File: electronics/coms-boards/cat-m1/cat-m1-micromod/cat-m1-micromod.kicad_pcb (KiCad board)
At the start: 2 copper layers, 37.5 x 65 mm, 56 parts, among them J1 MICROMOD_FUNCTION__STANDARD, J2 CONUFL001-SMD-T, J3 USB4145-03-0230-C_REVA, J4 SIM8060-6-0-14-00-A, Q1 BC847, Q2 BC847, SW1 1977223-6, U1 TPS22967DSGR, U2 SARA-R410M-02B, U3 AOZ8904CIL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

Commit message: updated to re-align with master
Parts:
- R2: value 1K -> 500
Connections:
- J1 pad 59: unconnected-(J1-Pad59) -> GND
- J1 pad 61: unconnected-(J1-Pad61) -> GND

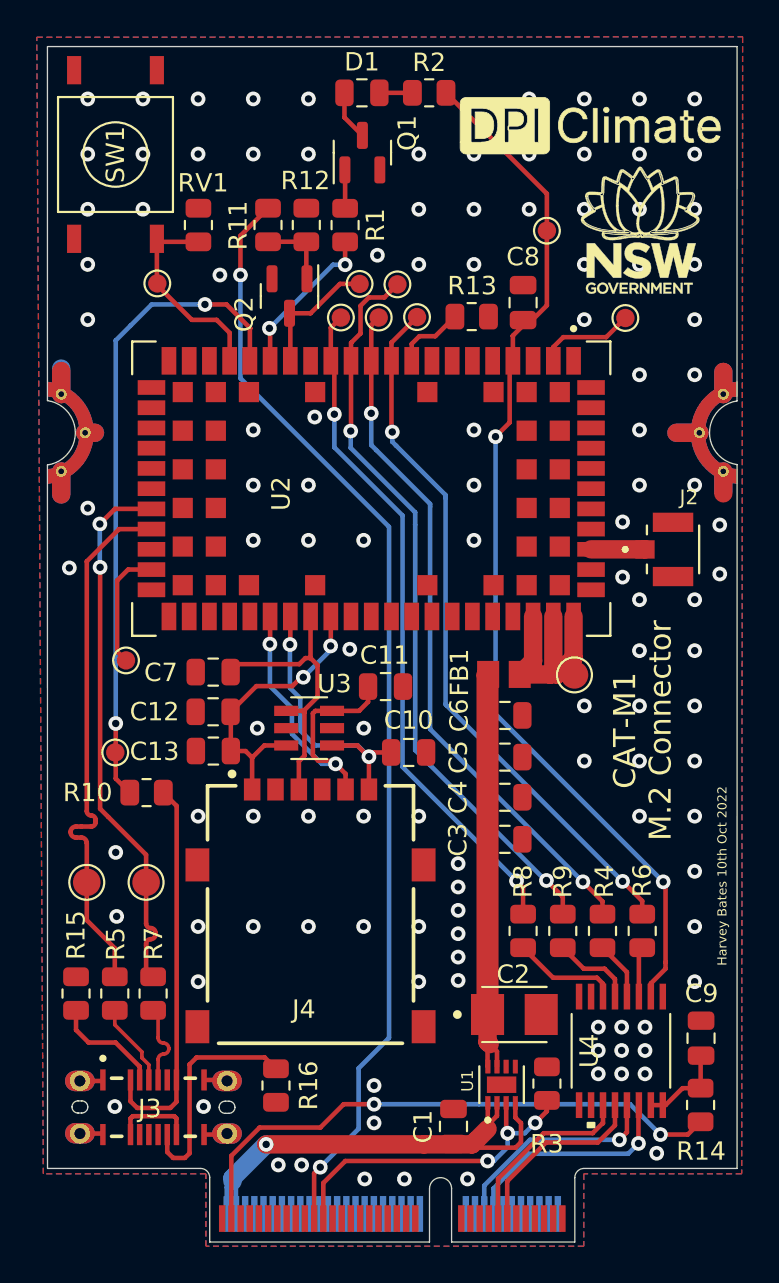
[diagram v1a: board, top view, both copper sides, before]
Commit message: realign with master branch before kangaroo board is split into seperate repo
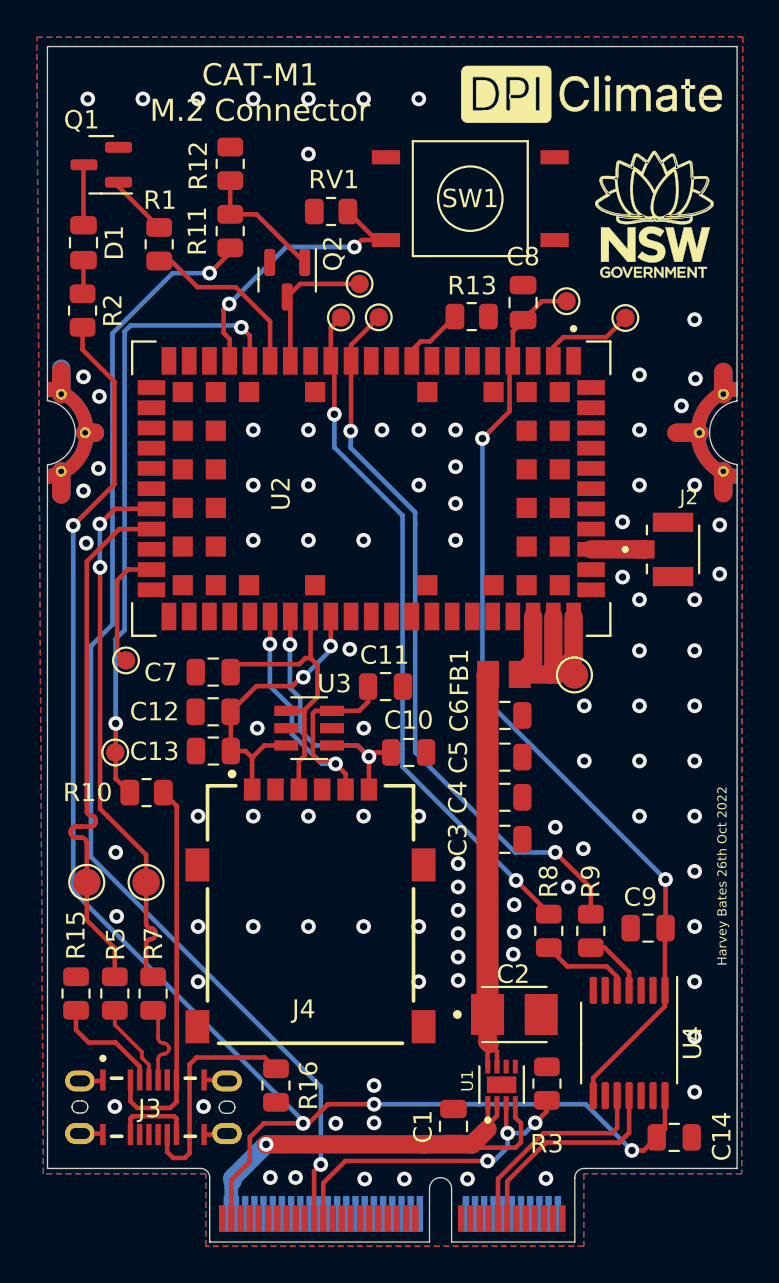
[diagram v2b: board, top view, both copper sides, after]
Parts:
- removed R14: 200K, Resistor_SMD:R_0805_2012Metric
- removed R4, R6: 0, Resistor_SMD:R_0805_2012Metric
- removed TP5: RTS_1V8, TestPoint:TestPoint_Pad_D1.0mm
- removed TP6: CTS_1V8, TestPoint:TestPoint_Pad_D1.0mm
- removed TP7: RESET_N, TestPoint:TestPoint_Pad_D1.0mm
- added C14: 0.1uF, Capacitor_SMD:C_0805_2012Metric, F.Cu at (115.9, 83.5)
- C9: value 1uF -> 0.1uF
- R2: value 500 -> 1.2K
- U4: value NVT2006PW -> TXB0104PW; footprint NVT2006PW:NVT2006PW -> Package_SO:TSSOP-14_4.4x5mm_P0.65mm
- moved R2 22.3 mm to (83.7, 38.5), turned to -90 degrees
- moved SW1 19.4 mm to (104.8, 32.4), turned to 180 degrees
- moved D1 17.2 mm to (83.8, 34.8), turned to -90 degrees
- moved Q1 14.2 mm to (84.7, 30.6), turned to 180 degrees
- moved R1 10.2 mm to (87.9, 34.9)
- moved RV1 7.25 mm to (97.2, 33.1), turned to 180 degrees
- moved C9 6.64 mm to (114.5, 72.1), turned to 180 degrees
- moved R12 5.31 mm to (91.7, 30.5)
- moved TP12 3.98 mm to (110.0, 38.0)
- moved R11 2.08 mm to (91.7, 34.2), turned to 90 degrees
- moved TP3 2.06 mm to (99.8, 38.9)
- moved R9 1.52 mm to (111.4, 72.2)
- moved R8 1.40 mm to (109.1, 72.2)
- moved Q2 0.90 mm to (94.8, 36.8)
- moved U4 0.62 mm to (113.4, 78.3)
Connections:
- C9 pad 1: Net-(C9-Pad1) -> +1V8
- J1 pad 16: RTS_3V3 -> unconnected-(J1-Pad16)
- J1 pad 18: CTS_3V3 -> unconnected-(J1-Pad18)
- R2 pad 2: +1V8 -> +3.3V
- SW1 pad 1: GND -> unconnected-(SW1-Pad1)
- SW1 pad 2: unconnected-(SW1-Pad2) -> GND
- U2 pad 10: Net-(R6-Pad2) -> GND
- U2 pad 11: Net-(R4-Pad2) -> unconnected-(U2-Pad11)
- U4 pad 1: GND -> +1V8
- U4 pad 10: unconnected-(U4-Pad10) -> RX_3V3
- U4 pad 11: RX_3V3 -> TX_3V3
- U4 pad 12: TX_3V3 -> unconnected-(U4-Pad12)
- U4 pad 13: CTS_3V3 -> unconnected-(U4-Pad13)
- U4 pad 14: RTS_3V3 -> +3.3V
- U4 pad 2: +1V8 -> unconnected-(U4-Pad2)
- U4 pad 3: RTS_1V8 -> unconnected-(U4-Pad3)
- U4 pad 4: CTS_1V8 -> TX_1V8
- U4 pad 5: TX_1V8 -> RX_1V8
- U4 pad 6: RX_1V8 -> unconnected-(U4-Pad6)
- U4 pad 7: unconnected-(U4-Pad7) -> GND
- U4 pad 8: unconnected-(U4-Pad8) -> +1V8
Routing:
- net +3.3V: track 31.1 -> 81.6 mm, vias 2 -> 4
- net Net-(R6-Pad2): track 38.7 -> 0.00 mm, vias 2 -> 0
- net Net-(R4-Pad2): track 37.8 -> 0.00 mm, vias 2 -> 0
- net RTS_3V3: track 12.4 -> 0.00 mm, vias 1 -> 0
- net CTS_3V3: track 12.0 -> 0.00 mm, vias 1 -> 0
- net +1V8: track 57.0 -> 51.6 mm
- net Net-(C9-Pad1): track 4.87 -> 0.00 mm
- net Net-(RV1-Pad1): track 11.4 -> 16.0 mm, vias 0 -> 2
- net CTS_1V8: track 3.21 -> 0.00 mm
- net Net-(Q2-Pad1): track 4.11 -> 6.97 mm
- net RTS_1V8: track 2.73 -> 0.00 mm
- net GPIO_PWR_ON: track 60.6 -> 62.4 mm
- net TX_3V3: track 10.2 -> 11.8 mm
- net RX_3V3: track 10.1 -> 11.5 mm
- net Net-(Q1-Pad1): track 2.09 -> 3.37 mm
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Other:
- board text added: "Harvey Bates 26th Oct 2022"
- board text removed: "Harvey Bates 10th Oct 2022"
